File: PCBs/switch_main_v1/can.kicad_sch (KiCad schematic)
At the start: 1 part, among them IC1001 TJA1055T_3_2Z

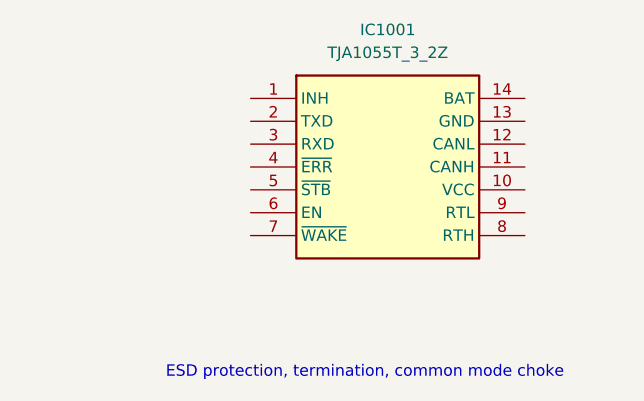
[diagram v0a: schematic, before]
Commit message: Connectors schematic almost complete
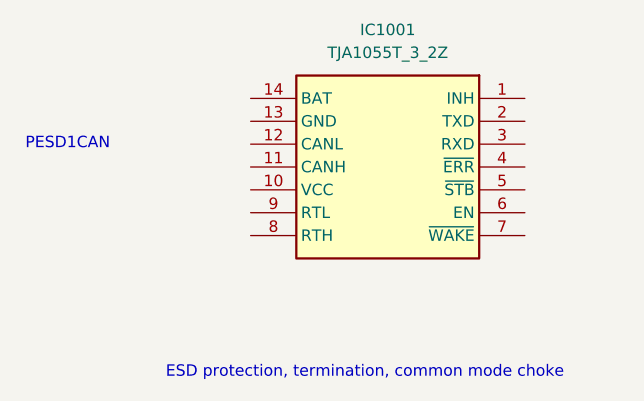
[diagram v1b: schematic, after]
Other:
- note added: "PESD1CAN"
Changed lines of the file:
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@@
 	(generator_version "8.0")
 	(paper "A4")
+	(text "PESD1CAN"
+		(exclude_from_sim no)
+		(at 119.38 99.06 0)
+		(effects
+			(font
+				(size 1.27 1.27)
+			)
+		)
+	)
 	(text "ESD protection, termination, common mode choke"
 		(exclude_from_sim no)
@@
 	(symbol
 		(lib_id "TJA1055T_3_2Z:TJA1055T_3_2Z")
-		(at 139.7 93.98 0)
+		(at 170.18 93.98 0)
+		(mirror y)
 		(unit 1)
 		(exclude_from_sim no)
@@
 		(on_board yes)
 		(dnp no)
-		(fields_autoplaced yes)
 		(property "Reference" "IC1001"
 			(at 154.94 86.36 0)
@@
 		)
 		(property "Footprint" "SOIC127P600X175-14N"
-			(at 166.37 188.9 0)
+			(at 143.51 188.9 0)
 			(effects
 				(font
@@
 		)
 		(property "Datasheet" "http://www.nxp.com/docs/en/data-sheet/TJA1055.pdf"
-			(at 166.37 288.9 0)
+			(at 143.51 288.9 0)
 			(effects
 				(font
@@
 		)
 		(property "Description" "CAN Interface IC Enhanced fault-tolerant CAN transceiver"
-			(at 139.7 93.98 0)
+			(at 170.18 93.98 0)
 			(effects
 				(font
@@
 		)
 		(property "Height" "1.75"
-			(at 166.37 488.9 0)
+			(at 143.51 488.9 0)
 			(effects
 				(font
@@
 		)
 		(property "Mouser Part Number" "771-TJA1055T/3/2Z"
-			(at 166.37 588.9 0)
+			(at 143.51 588.9 0)
 			(effects
 				(font
@@
 		)
 		(property "Mouser Price/Stock" "https://www.mouser.co.uk/ProductDetail/NXP-Semiconductors/TJA1055T-3-2Z?qs=qSfuJ%252Bfl%2Fd73Y%2FIsMw3Ayg%3D%3D"
-			(at 166.37 688.9 0)
+			(at 143.51 688.9 0)
 			(effects
 				(font
@@
 		)
 		(property "Manufacturer_Name" "NXP"
-			(at 166.37 788.9 0)
+			(at 143.51 788.9 0)
 			(effects
 				(font
@@
 		)
 		(property "Manufacturer_Part_Number" "TJA1055T/3/2Z"
-			(at 166.37 888.9 0)
+			(at 143.51 888.9 0)
 			(effects
 				(font

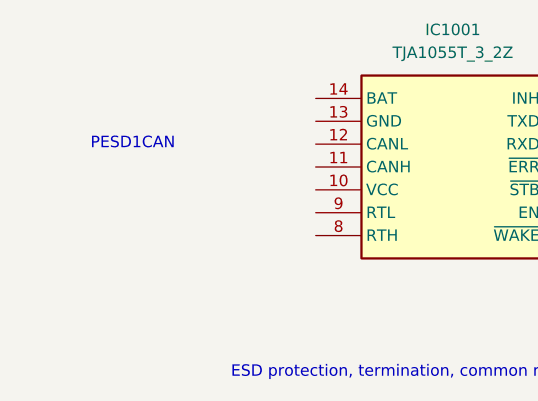
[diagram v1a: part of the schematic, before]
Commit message: Added schematic annotations
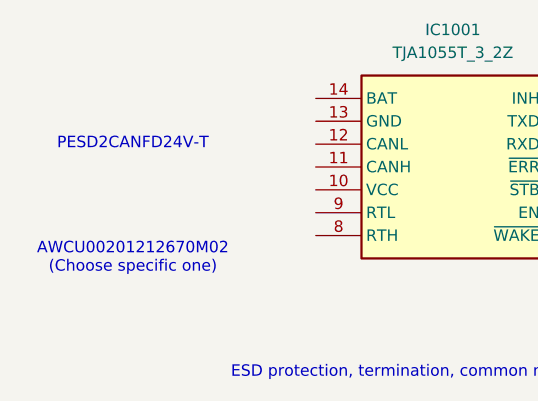
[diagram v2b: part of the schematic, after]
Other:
- note added: "AWCU00201212670M02 (Choose specific one)"
- note added: "PESD2CANFD24V-T"
- note removed: "PESD1CAN"
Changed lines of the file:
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@@
 	(generator_version "8.0")
 	(paper "A4")
-	(text "PESD1CAN"
+	(text "AWCU00201212670M02\n(Choose specific one)"
+		(exclude_from_sim no)
+		(at 119.38 111.76 0)
+		(effects
+			(font
+				(size 1.27 1.27)
+			)
+		)
+	)
+	(text "PESD2CANFD24V-T"
 		(exclude_from_sim no)
 		(at 119.38 99.06 0)

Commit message: Schematic progress
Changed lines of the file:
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@@
 	(text "AWCU00201212670M02\n(Choose specific one)"
 		(exclude_from_sim no)
-		(at 119.38 111.76 0)
+		(at 73.66 109.22 0)
 		(effects
 			(font
@@
 	(text "PESD2CANFD24V-T"
 		(exclude_from_sim no)
-		(at 119.38 99.06 0)
+		(at 73.66 96.52 0)
 		(effects
 			(font

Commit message: GbE part of schematic done
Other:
- company: (none) -> Ben Smith
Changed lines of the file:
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@@
 		(date "2024-04-06")
 		(rev "0.0.0")
+		(company "Ben Smith")
 	)
 	(text "AWCU00201212670M02\n(Choose specific one)"

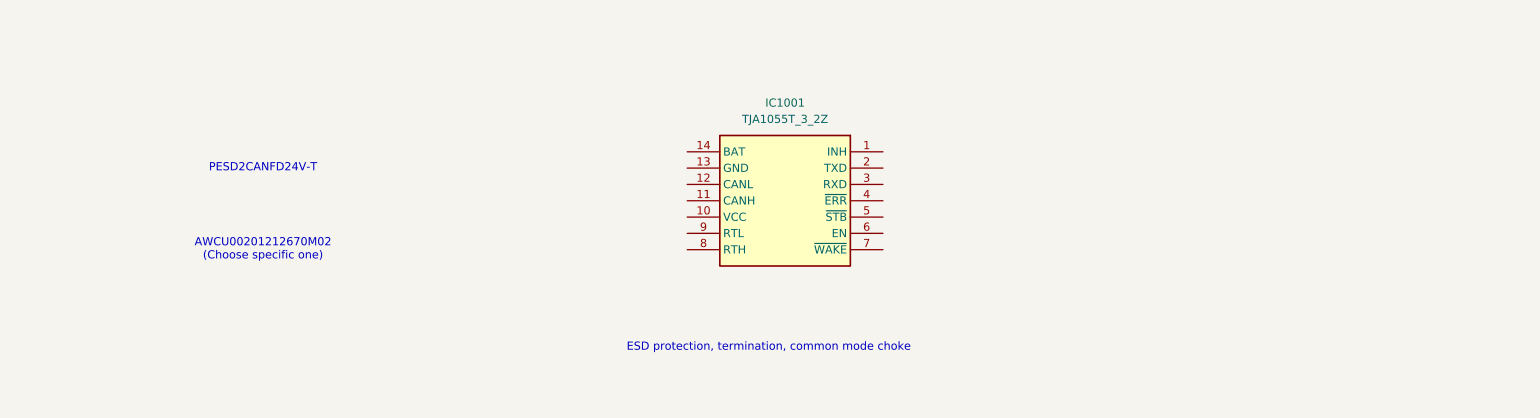
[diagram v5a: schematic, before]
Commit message: Progress on CAN schematic sheet
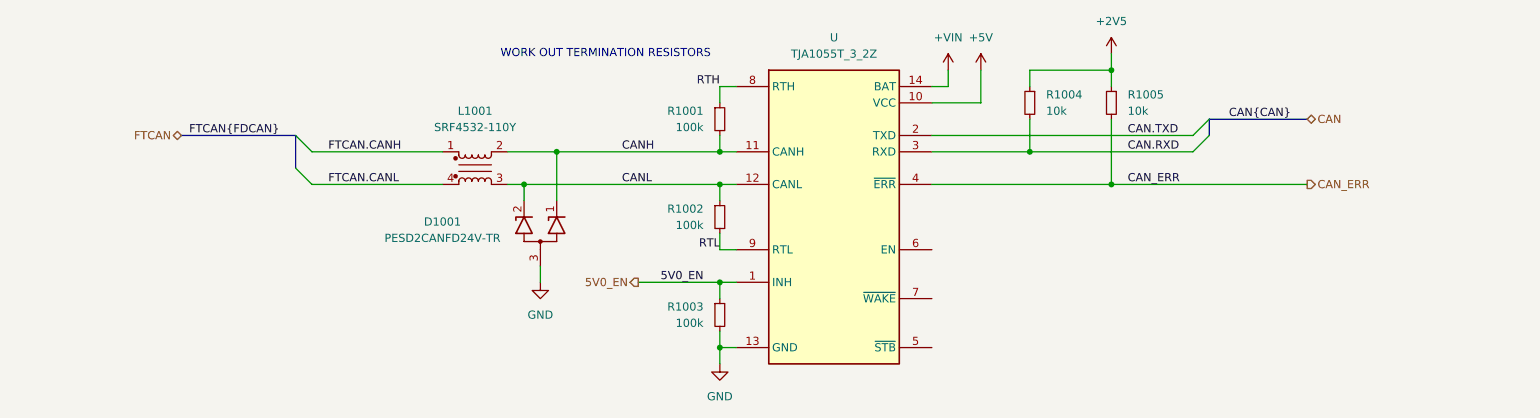
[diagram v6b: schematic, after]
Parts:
- added D1001: PESD2CANFD24V-TR, switch_footprints:SOT95P230X110-3N, symbol PESD2CANFD24V-TR:PESD2CANFD24V-TR
- added L1001: SRF4532-110Y, switch_footprints:SRF4532101Y, symbol SRF4532-110Y:SRF4532-110Y
- added R1001, R1002, R1003: 100k, Resistor_SMD:R_0402_1005Metric, symbol Device:R_Small
- added R1004, R1005: 10k, Resistor_SMD:R_0402_1005Metric, symbol Device:R_Small
- U: renamed from IC1001; footprint SOIC127P600X175-14N -> switch_footprints:SOIC127P600X175-14N
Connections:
- net 5V0_EN: now reaches U.1 (INH)
- net 5V0_EN: now also R1003.1
- net +5V: now reaches U.10 (VCC)
- net CANH: now reaches U.11 (CANH)
- net CANH: now also D1001.1 (K1), L1001.2, R1001.2
- net CANL: now reaches U.12 (CANL)
- net CANL: now also D1001.2 (K2), L1001.3, R1002.1
- net GND: now reaches U.13 (GND)
- net GND: now also D1001.3 (CC), R1003.2
- net +VIN: now reaches U.14 (BAT)
- net CAN.TXD: now reaches U.2 (TXD)
- net CAN.RXD: now reaches U.3 (RXD)
- net CAN.RXD: now also R1004.2
- net CAN_ERR: now reaches U.4 (~{ERR})
- net CAN_ERR: now also R1005.2
- net RTH: now reaches U.8 (RTH)
- net RTH: now also R1001.1
- net RTL: now reaches U.9 (RTL)
- net RTL: now also R1002.2
- new net +2V5: R1004.1, R1005.1
- new net FTCAN.CANH: L1001.1
- new net FTCAN.CANL: L1001.4
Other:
- note added: "WORK OUT TERMINATION RESISTORS"
- note removed: "AWCU00201212670M02 (Choose specific one)"
- note removed: "ESD protection, termination, common mode choke"
- note removed: "PESD2CANFD24V-T"
- moved on the sheet: U

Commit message: Changed MCU to STM32H573VIT3Q
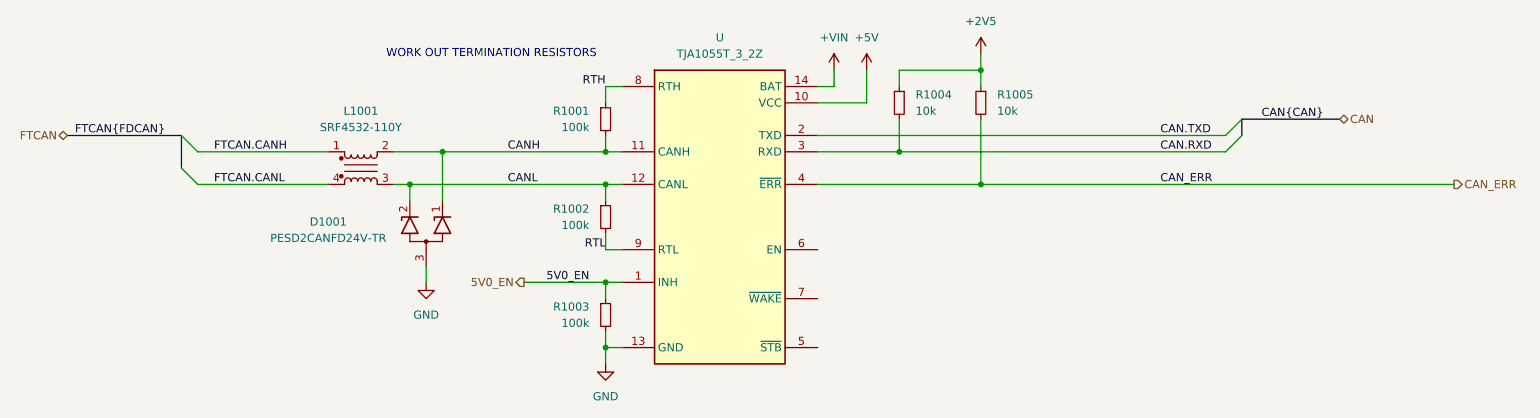
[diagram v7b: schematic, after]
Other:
- moved on the sheet: D1001, L1001, R1001, R1002, R1003, R1004, R1005, U

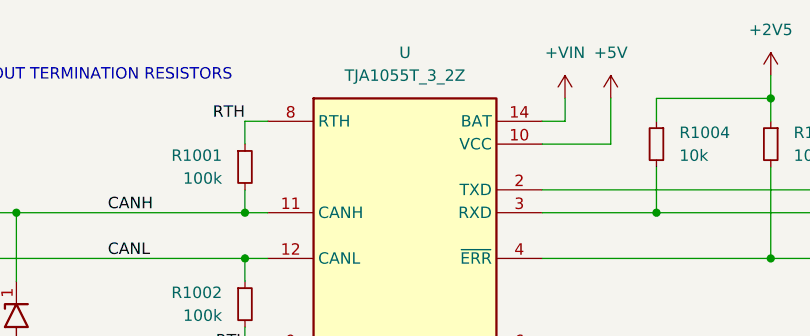
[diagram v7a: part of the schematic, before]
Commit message: Changed MCU to STM32H573IIK3Q
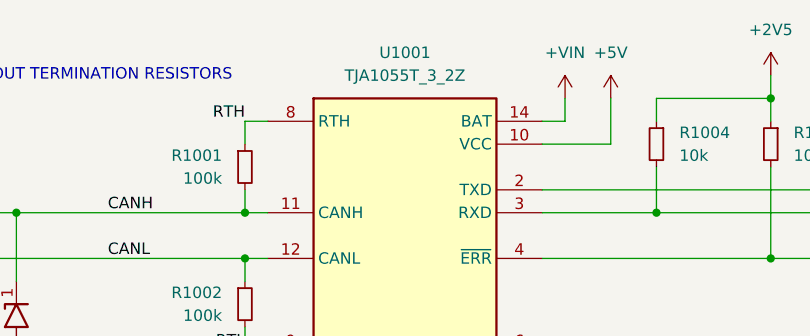
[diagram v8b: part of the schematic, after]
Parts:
- renumbered U to U1001
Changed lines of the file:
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@@
 		(on_board yes)
 		(dnp no)
-		(property "Reference" "U"
+		(property "Reference" "U1001"
 			(at 144.78 76.2 0)
 			(effects
@@
 			(project "switch_main_v1"
 				(path "/4638d344-96ef-43ce-a37a-2df37185796e/b422119d-484b-4264-b790-e0e08cc5012d"
-					(reference "U")
+					(reference "U1001")
 					(unit 1)
 				)
@@
 			)
 		)
-		(property "Description" "Power symbol creates a global label with name \"+VIN\""
+		(property "Description" "Power symbol creates a global label with name \"+5V\""
 			(at 162.56 81.28 0)
 			(effects
